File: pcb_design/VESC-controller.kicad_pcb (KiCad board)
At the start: 2 copper layers, 160 x 92.5 mm, 183 parts, among them J1 GATE_DRIVER_CONN_U, J2 GATE_DRIVER_CONN_V, J3 GATE_DRIVER_CONN_W, J4 micro USB, J5 ACCEL, J6 REGEN, J7 12V, P1 HALL/Encoder, P101 CANBUS, P3 PWR_COMM, Q1 BSC340N08, U1 STM32F40X_LQFP64, U10 LM2903-SO8, U11 LM3488, U12 OPA2376AID, U13 LM1117IMP-v.v, U16 OPA2376AID, U17 LM2903-SO8, U2 ISO1050, U3 OPA2376AID, U4 LM2903-SO8, U5 7400-TSSOP, U6 SN74ALVC08PWR, U7 SN74ALVC08PWR, U8 SN74AUP1G74, U9 LM22676QTJ-5.0, X2 ABM3B - 8MHz

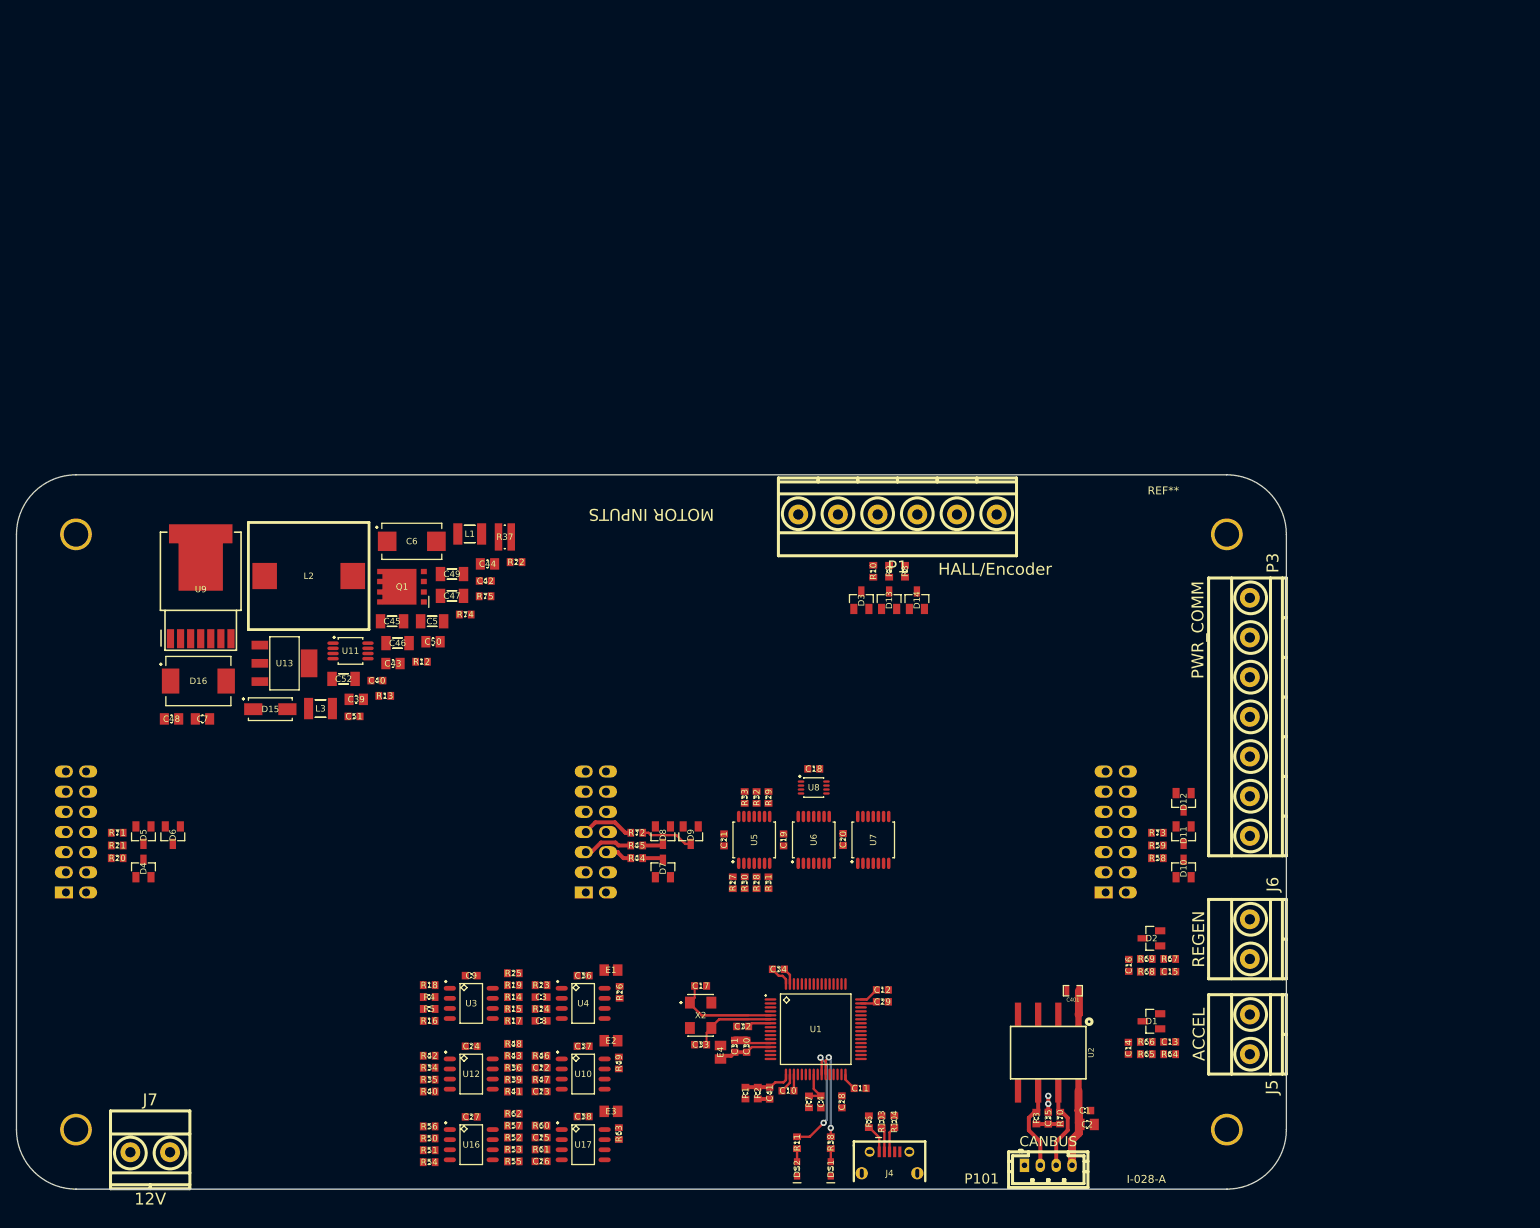
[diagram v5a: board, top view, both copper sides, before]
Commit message: Fixed issue with non-bidirectional phase current measurement. Started routing power supplies. Changed terminal blocks from 5.00mm to 3.81mm pitch
Signed-off-by: Marcos Chaparro <mchaparro@paltatech.com>
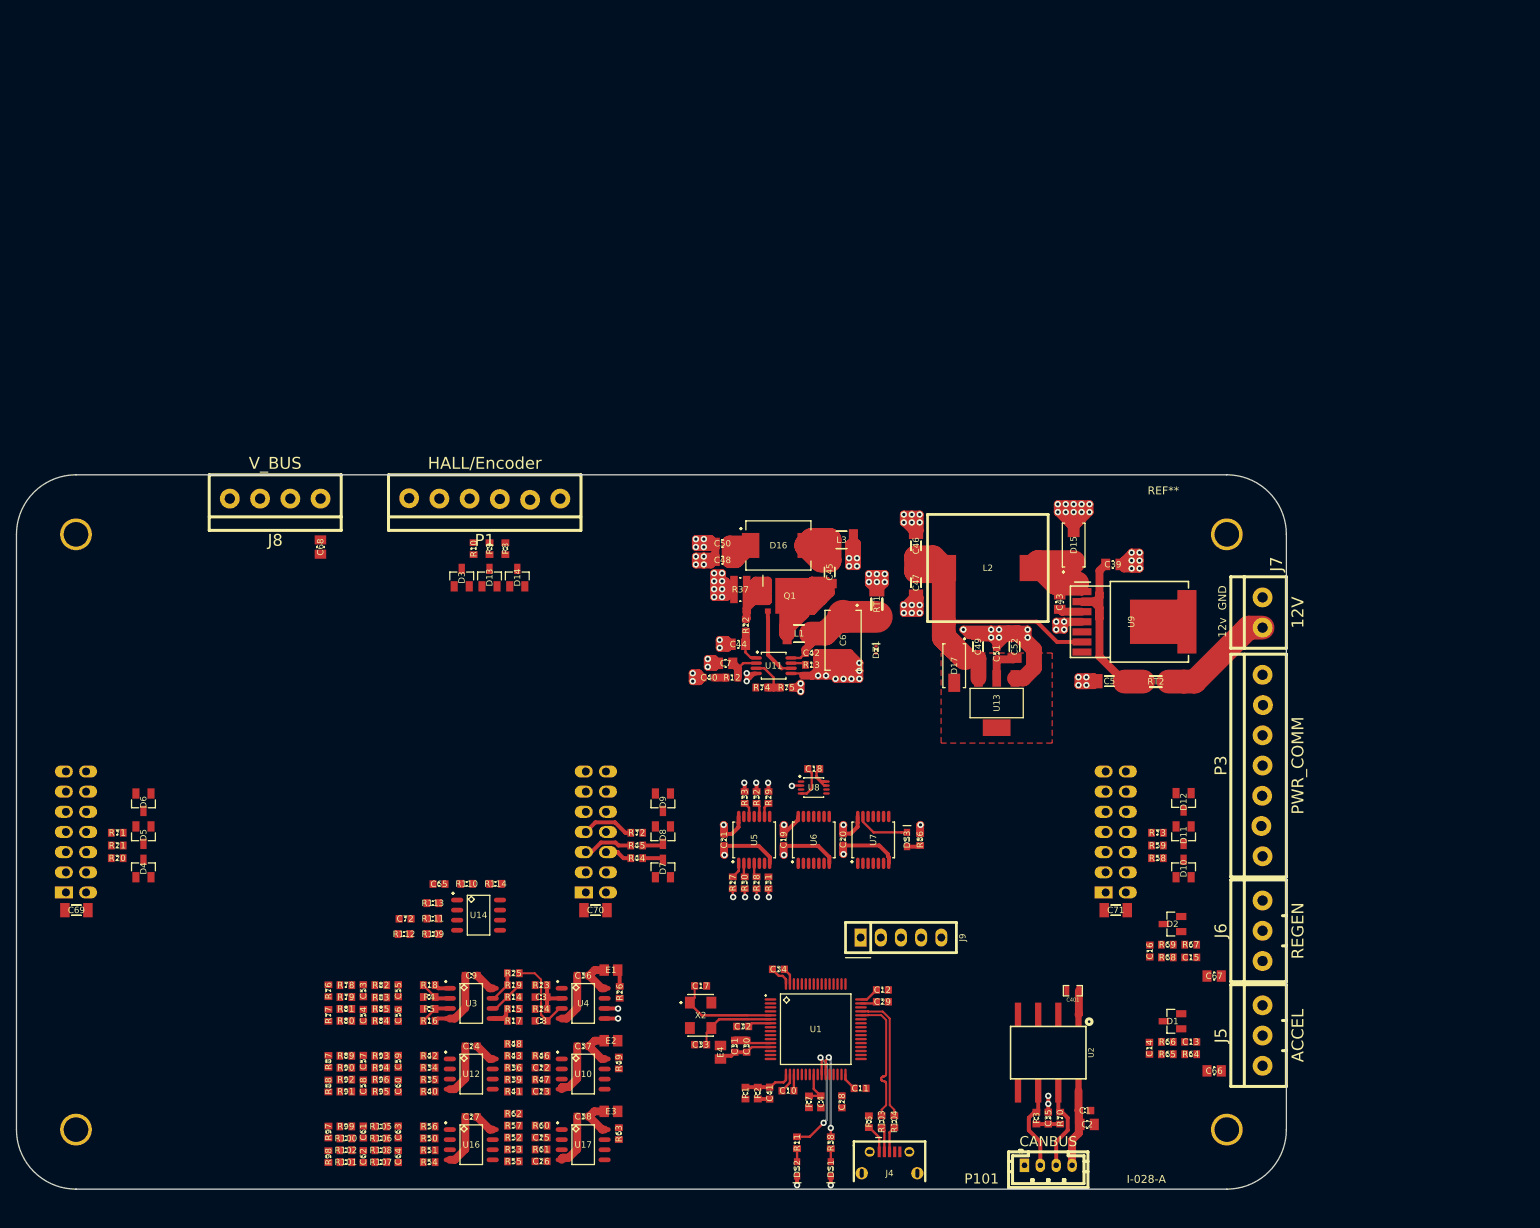
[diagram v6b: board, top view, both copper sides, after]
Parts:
- added C53: 100pF, IPC7351-Nominal:CAPC1608X55, F.Cu at (-36.3, 20.0)
- added C54: 100pF, IPC7351-Nominal:CAPC1608X55, F.Cu at (-36.3, 23.1)
- added C55: 100pF, IPC7351-Nominal:CAPC1608X55, F.Cu at (-31.9, 20.0)
- added C56: 100pF, IPC7351-Nominal:CAPC1608X55, F.Cu at (-31.9, 23.1)
- added C57: 100pF, IPC7351-Nominal:CAPC1608X55, F.Cu at (-36.3, 28.9)
- added C58: 100pF, IPC7351-Nominal:CAPC1608X55, F.Cu at (-36.3, 32.0)
- added C59: 100pF, IPC7351-Nominal:CAPC1608X55, F.Cu at (-31.9, 28.9)
- added C60: 100pF, IPC7351-Nominal:CAPC1608X55, F.Cu at (-31.9, 32.0)
- added C61: 100pF, IPC7351-Nominal:CAPC1608X55, F.Cu at (-36.3, 37.8)
- added C62: 100pF, IPC7351-Nominal:CAPC1608X55, F.Cu at (-36.3, 40.9)
- added C63: 100pF, IPC7351-Nominal:CAPC1608X55, F.Cu at (-31.9, 37.8)
- added C64: 100pF, IPC7351-Nominal:CAPC1608X55, F.Cu at (-31.9, 40.9)
- added C65: 100pF, IPC7351-Nominal:CAPC1608X55, F.Cu at (-26.8, 6.56)
- added C66: 4.7uF, IPC7351-Nominal:CAPC2012X70, F.Cu at (70.9, 30.1)
- added C67: 4.7uF, IPC7351-Nominal:CAPC2012X70, F.Cu at (70.9, 18.1)
- added C68: 4.7uF, IPC7351-Nominal:CAPC2012X70, F.Cu at (-41.7, -35.9)
- added C69: 4.7uF 50v, IPC7351-Nominal:CAPC3216X70, F.Cu at (-72.5, 9.85)
- added C70: 4.7uF 50v, IPC7351-Nominal:CAPC3216X70, F.Cu at (-7.05, 9.85)
- added C71: 4.7uF 50v, IPC7351-Nominal:CAPC3216X70, F.Cu at (58.5, 9.85)
- added C72: 100nF, IPC7351-Nominal:CAPC1608X55, F.Cu at (-31.0, 10.9)
- added D17: SS16, IPC7351-Nominal:DIOM5326X292, F.Cu at (38.1, -20.9)
- added DS3: OCP, smd-semi:LED-0603, F.Cu at (32.2, 0.95)
- added DZ1: ESD9L5.0ST5G, smd-semi:SOD-THAT, F.Cu at (28.3, -22.9)
- added J8: V_BUS, conn-phoenix:mcv_1,5-4-G-3,81, F.Cu at (-47.4, -42.0)
- added J9: SWD, conn-100mil:CONN-100MIL-M-1x5, F.Cu at (31.4, 13.3)
- added R100: 100R, IPC7351-Nominal:RESC1608X50, F.Cu at (-38.5, 38.6)
- added R101: 100R, IPC7351-Nominal:RESC1608X50, F.Cu at (-38.5, 41.6)
- added R102: 100R, IPC7351-Nominal:RESC1608X50, F.Cu at (-38.5, 40.1)
- added R105: 100R, IPC7351-Nominal:RESC1608X50, F.Cu at (-34.1, 37.1)
- added R106: 100R, IPC7351-Nominal:RESC1608X50, F.Cu at (-34.1, 38.6)
- added R107: 100R, IPC7351-Nominal:RESC1608X50, F.Cu at (-34.1, 41.6)
- added R108: 100R, IPC7351-Nominal:RESC1608X50, F.Cu at (-34.1, 40.1)
- added R109: 100R, IPC7351-Nominal:RESC1608X50, F.Cu at (-27.5, 12.9)
- added R110: 100R, IPC7351-Nominal:RESC1608X50, F.Cu at (-23.3, 6.54)
- added R111: 10k, IPC7351-Nominal:RESC1608X50, F.Cu at (-27.5, 10.9)
- added R112: 10k, IPC7351-Nominal:RESC1608X50, F.Cu at (-31.2, 12.9)
- added R113: 10k, IPC7351-Nominal:RESC1608X50, F.Cu at (-27.5, 8.97)
- added R114: 10k, IPC7351-Nominal:RESC1608X50, F.Cu at (-19.6, 6.54)
- added R76: 2k, IPC7351-Nominal:RESC1608X50, F.Cu at (-40.7, 20.0)
- added R77: 2k, IPC7351-Nominal:RESC1608X50, F.Cu at (-40.7, 23.1)
- added R78: 100R, IPC7351-Nominal:RESC1608X50, F.Cu at (-38.5, 19.3)
- added R79: 100R, IPC7351-Nominal:RESC1608X50, F.Cu at (-38.5, 20.8)
- added R80: 100R, IPC7351-Nominal:RESC1608X50, F.Cu at (-38.5, 23.8)
- added R81: 100R, IPC7351-Nominal:RESC1608X50, F.Cu at (-38.5, 22.3)
- added R82: 100R, IPC7351-Nominal:RESC1608X50, F.Cu at (-34.1, 19.3)
- added R83: 100R, IPC7351-Nominal:RESC1608X50, F.Cu at (-34.1, 20.8)
- added R84: 100R, IPC7351-Nominal:RESC1608X50, F.Cu at (-34.1, 23.8)
- added R85: 100R, IPC7351-Nominal:RESC1608X50, F.Cu at (-34.1, 22.3)
- added R86: 100R, IPC7351-Nominal:RESC1608X50, F.Cu at (33.9, 0.95)
- added R87: 2k, IPC7351-Nominal:RESC1608X50, F.Cu at (-40.7, 28.9)
- added R88: 2k, IPC7351-Nominal:RESC1608X50, F.Cu at (-40.7, 32.0)
- added R89: 100R, IPC7351-Nominal:RESC1608X50, F.Cu at (-38.5, 28.2)
- added R90: 100R, IPC7351-Nominal:RESC1608X50, F.Cu at (-38.5, 29.7)
- added R91: 100R, IPC7351-Nominal:RESC1608X50, F.Cu at (-38.5, 32.7)
- added R92: 100R, IPC7351-Nominal:RESC1608X50, F.Cu at (-38.5, 31.2)
- added R93: 100R, IPC7351-Nominal:RESC1608X50, F.Cu at (-34.1, 28.2)
- added R94: 100R, IPC7351-Nominal:RESC1608X50, F.Cu at (-34.1, 29.7)
- added R95: 100R, IPC7351-Nominal:RESC1608X50, F.Cu at (-34.1, 32.7)
- added R96: 100R, IPC7351-Nominal:RESC1608X50, F.Cu at (-34.1, 31.2)
- added R97: 2k, IPC7351-Nominal:RESC1608X50, F.Cu at (-40.7, 37.8)
- added R98: 2k, IPC7351-Nominal:RESC1608X50, F.Cu at (-40.7, 40.9)
- added R99: 100R, IPC7351-Nominal:RESC1608X50, F.Cu at (-38.5, 37.1)
- added RT1: POLYFUSE-30R500, IPC7351-Most:RESC3216X60, F.Cu at (28.4, -28.7)
- added RT2: POLYFUSE-30R500, IPC7351-Most:RESC3216X60, F.Cu at (63.5, -18.9)
- added U14: OPA2376AID, IPC7351-Nominal:SOIC127P600X175-8, F.Cu at (-21.8, 10.5)
- J5, J6: footprint w_conn_mkds:mkds_1,5-2 -> conn-phoenix:mcv_1,5-3-G-3,81
- J7: footprint w_conn_mkds:mkds_1,5-2 -> conn-phoenix:mcv_1,5-2-G-3,81
- P1: footprint w_conn_mkds:mkds_1,5-6 -> conn-phoenix:mcv_1,5-6-G-3,81
- P3: footprint w_conn_mkds:mkds_1,5-7 -> conn-phoenix:mcv_1,5-7-G-3,81
- REF**: footprint paltatech:VESC-controller-outline -> VESC-controller-outline
- moved J7 155.8 mm to (77.0, -27.6), turned to 90 degrees
- moved U9 117.3 mm to (60.5, -26.5), turned to 270 degrees
- moved D15 103.3 mm to (53.2, -36.1), turned to 90 degrees
- moved C39 96.8 mm to (58.1, -33.7)
- moved U13 89.9 mm to (43.5, -16.2), turned to 270 degrees
- moved C5 85.7 mm to (57.7, -19.0), turned to 180 degrees
- moved L2 85.6 mm to (42.4, -33.3)
- moved C52 84.6 mm to (45.8, -23.4), turned to 270 degrees
- moved C43 84.4 mm to (51.4, -29.0), turned to 270 degrees
- moved C51 81.4 mm to (43.5, -22.5), turned to 90 degrees
- moved D16 75.1 mm to (16.0, -36.1)
- moved C48 72.2 mm to (8.95, -34.2), turned to 180 degrees
- moved L3 69.0 mm to (23.9, -36.8), turned to 180 degrees
- moved C49 66.9 mm to (41.1, -23.4), turned to 90 degrees
- moved C46 66.5 mm to (33.3, -36.1), turned to 90 degrees
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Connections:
- net /STM32F4/SPI3_MISO renamed /STM32F4/PC11
- net /STM32F4/SPI3_SCK renamed /STM32F4/PC10
- net /STM32F4/USB_DM renamed /STM32F4/USB_D-
- net /STM32F4/USB_DP renamed /STM32F4/USB_D+
- net /Supervisor/DRIVER_RESET_OUT renamed /Supervisor/~DRIVER_RST_OUT
- net 24v renamed +24
- C10 pad 1: VCC -> +3.3
- C11 pad 1: VCC -> +3.3
- C12 pad 1: VCC -> +3.3
- C18 pad 2: VCC -> +3.3
- C19 pad 2: VCC -> +3.3
- C20 pad 2: VCC -> +3.3
- C21 pad 2: VCC -> +3.3
- C30 pad 1: Net-(C30-Pad1) -> +3.3A
- C31 pad 1: Net-(C30-Pad1) -> +3.3A
- C34 pad 1: VCC -> +3.3
- C39 pad 1: /Power/12v_in -> Net-(C39-Pad1)
- C401 pad 1: VCC -> +3.3
- C42 pad 1: /Power/12v_in -> Net-(C42-Pad1)
- C46 pad 1: 5.0v -> +5
- C47 pad 1: 5.0v -> +5
- C49 pad 1: 5.0v -> +5
- C5 pad 1: /Power/12v_in -> Net-(C39-Pad1)
- C51 pad 1: 3.3v -> +3.3
- C52 pad 2: 3.3v -> +3.3
- C6 pad 1: /Power/12v_in -> Net-(C42-Pad1)
- D10 pad 2: VCC -> +3.3
- D11 pad 2: VCC -> +3.3
- D12 pad 2: VCC -> +3.3
- D13 pad 2: VCC -> +3.3
- D14 pad 2: VCC -> +3.3
- D3 pad 2: VCC -> +3.3
- D4 pad 2: VCC -> +3.3
- D5 pad 2: VCC -> +3.3
- D6 pad 2: VCC -> +3.3
- D7 pad 2: VCC -> +3.3
- D8 pad 2: VCC -> +3.3
- D9 pad 2: VCC -> +3.3
- E1 pad 2: VCC -> +3.3
- E2 pad 2: VCC -> +3.3
- E3 pad 2: VCC -> +3.3
- E4 pad 1: Net-(C30-Pad1) -> +3.3A
- E4 pad 2: VCC -> +3.3
- J5 pad 1: /Accel input conditioning/IN -> +5
- J5 pad 2: GND -> /Accel input conditioning/IN
- J6 pad 1: /Regen input conditioning/IN -> +5
- J6 pad 2: GND -> /Regen input conditioning/IN
- L1 pad 2: /Power/12v_in -> Net-(C42-Pad1)
- L2 pad 1: 5.0v -> +5
- P1 pad 1: +5V -> +5
- P3 pad 1: +5V -> +5
- P3 pad 2: VCC -> +3.3
- R1 pad 1: VCC -> +3.3A
- R14 pad 2: /conditioning U/I_phase+ -> Net-(C56-Pad1)
- R15 pad 2: /conditioning U/I_phase- -> Net-(C56-Pad2)
- R26 pad 2: VCC -> +3.3
- R33 pad 1: VCC -> +3.3
- R34 pad 2: /conditioning V/V_phase+ -> Net-(C59-Pad1)
- R35 pad 2: /conditioning V/V_phase- -> Net-(C59-Pad2)
- R36 pad 2: /conditioning V/I_phase+ -> Net-(C60-Pad1)
- R39 pad 2: /conditioning V/I_phase- -> Net-(C60-Pad2)
- R4 pad 2: /conditioning U/V_phase+ -> Net-(C55-Pad1)
- R49 pad 2: VCC -> +3.3
- R5 pad 2: /conditioning U/V_phase- -> Net-(C55-Pad2)
- R50 pad 2: /conditioning W/V_phase+ -> Net-(C63-Pad1)
- R51 pad 2: /conditioning W/V_phase- -> Net-(C63-Pad2)
- R52 pad 2: /conditioning W/I_phase+ -> Net-(C64-Pad1)
- R53 pad 2: /conditioning W/I_phase- -> Net-(C64-Pad2)
- R6 pad 2: +5V -> +5
- R63 pad 2: VCC -> +3.3
- R7 pad 2: VCC -> +3.3
- U1 pad 1: VCC -> +3.3
- U1 pad 11: /STM32F4/AN_IN -> /Vbus_conditioning/OUT
- U1 pad 13: Net-(C30-Pad1) -> +3.3A
- U1 pad 19: VCC -> +3.3
- U1 pad 32: VCC -> +3.3
- U1 pad 33: /STM32F4/PB12 -> /STM32F4/~FAULT
- U1 pad 40: /STM32F4/SPI3_CS -> SUPPLY_SYNC
- U1 pad 48: VCC -> +3.3
- U1 pad 53: /STM32F4/SPI3_MOSI -> /Supervisor/CLR_OC_Fault
- U1 pad 56: /STM32F4/PB4 -> -VEE_ctrl
- U1 pad 58: -VEE_ctrl -> /STM32F4/PWM_AUX
- U1 pad 59: FAULT -> /Supervisor/OC_Fault
- U1 pad 64: VCC -> +3.3
- U10 pad 5: Net-(U10-Pad5) -> GND
- U10 pad 6: Net-(U10-Pad6) -> +3.3
- U11 pad 8: /Power/12v_in -> Net-(C42-Pad1)
- U13 pad 2: 3.3v -> +3.3
- U13 pad 3: 5.0v -> +5
- U13 pad 4: 3.3v -> +3.3
- U17 pad 5: Net-(U17-Pad5) -> GND
- U17 pad 6: Net-(U17-Pad6) -> +3.3
- U2 pad 1: VCC -> +3.3
- U4 pad 5: Net-(U4-Pad5) -> GND
- U4 pad 6: Net-(U4-Pad6) -> +3.3
- U5 pad 14: VCC -> +3.3
- U6 pad 14: VCC -> +3.3
- U7 pad 10: FAULT -> /STM32F4/~FAULT
- U7 pad 14: VCC -> +3.3
- U7 pad 9: /Supervisor/DRIVER_RESET_IN -> /STM32F4/~DRIVER_RESET
- U8 pad 2: VCC -> +3.3
- U8 pad 6: /Supervisor/CLEAR_OC_Fault -> /Supervisor/CLR_OC_Fault
- U8 pad 7: VCC -> +3.3
- U8 pad 8: VCC -> +3.3
- U9 pad 2: /Power/12v_in -> Net-(C39-Pad1)
- U9 pad 6: 5.0v -> +5
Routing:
- net GND: track 10.7 -> 315.7 mm, vias 0 -> 93
- net /Power/12v_in: track 0.00 -> 92.0 mm, vias 0 -> 6
- net +5: track 0.00 -> 46.5 mm
- net +3.3: track 0.00 -> 43.1 mm, vias 0 -> 7
- net Net-(C45-Pad2): track 0.00 -> 40.0 mm
- net Net-(C39-Pad1): track 0.00 -> 25.6 mm
- net Net-(Q1-Pad1): track 0.00 -> 25.0 mm
- net /STM32F4/USB_D-: track 0.00 -> 16.5 mm
- net /STM32F4/USB_D+: track 0.00 -> 16.5 mm
- net Net-(C43-Pad1): track 0.00 -> 16.4 mm
- net Net-(C42-Pad1): track 0.00 -> 14.1 mm
- net Net-(C8-Pad1): track 0.00 -> 12.6 mm
- net VCC: track 12.6 -> 0.00 mm
- net Net-(C45-Pad1): track 0.00 -> 9.58 mm
- net Net-(Q1-Pad4): track 0.00 -> 9.16 mm
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- added copper zone on F.Cu, net +3.3
- added copper zone on PWR.Cu, net +3.3
- added copper zone on GND.Cu, net GND
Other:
- board size 160 x 92.5 mm -> 160 x 90 mm
- copper layers 2 -> 4
- rule pad_to_mask_clearance: 0.2 -> 0.15
- board text added: "12v"
- board text added: "GND"
- board text removed: "MOTOR INPUTS"

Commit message: More layout
Signed-off-by: Marcos Chaparro <mchaparro@paltatech.com>
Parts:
- added P2: Resolver, conn-phoenix:mcv_1,5-6-G-3,81, F.Cu at (-5.00, -42.0)
- added R115: 1k, IPC7351-Nominal:RESC1608X50, F.Cu at (-16.2, 34.4)
- added R116: 1k, IPC7351-Nominal:RESC1608X50, F.Cu at (-16.2, 37.2)
- added R117: 1k, IPC7351-Nominal:RESC1608X50, F.Cu at (-16.2, 25.6)
- added R118: 1k, IPC7351-Nominal:RESC1608X50, F.Cu at (-16.2, 28.7)
- added R119: 1k, IPC7351-Nominal:RESC1608X50, F.Cu at (-16.9, 17.2)
- added R120: 1k, IPC7351-Nominal:RESC1608X50, F.Cu at (-16.9, 20.1)
- added R121: 2k, IPC7351-Nominal:RESC1608X50, F.Cu at (-36.1, 7.95)
- added R122: 1k, IPC7351-Nominal:RESC1608X50, F.Cu at (23.4, 13.2)
- J1, J2, J3: footprint conn-100mil:CONN-100MIL-M-2x7 -> conn-100mil:CONN-100MIL-M-2x8
- R17, R41, R55: value R-0603 -> 9.5k
- moved R50 20.8 mm to (-29.8, 17.9)
- moved R51 20.8 mm to (-29.8, 19.4)
- moved R54 20.8 mm to (-29.8, 20.9)
- moved R56 20.8 mm to (-29.8, 16.4)
- moved C27 20.8 mm to (-24.4, 15.2)
- moved R52 20.8 mm to (-19.1, 17.8)
- moved R53 20.8 mm to (-19.1, 19.3)
- moved R55 20.8 mm to (-19.1, 20.8)
- moved R57 20.8 mm to (-19.1, 16.3)
- moved R62 20.8 mm to (-19.1, 14.8)
- moved U16 20.8 mm to (-24.4, 18.7)
- moved R100 20.7 mm to (-39.5, 17.9)
- moved R101 20.7 mm to (-39.5, 20.9)
- moved R102 20.7 mm to (-39.5, 19.4)
- moved R105 20.7 mm to (-35.1, 16.4)
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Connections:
- net Net-(C55-Pad1) renamed /conditioning U/V_diff_+
- net Net-(C55-Pad2) renamed /conditioning U/V_diff_-
- net Net-(C56-Pad1) renamed /conditioning U/I_diff_+
- net Net-(C56-Pad2) renamed /conditioning U/I_diff_-
- net Net-(C59-Pad1) renamed /conditioning V/V_diff_+
- net Net-(C59-Pad2) renamed /conditioning V/V_diff_-
- net Net-(C60-Pad1) renamed /conditioning V/I_diff_+
- net Net-(C60-Pad2) renamed /conditioning V/I_diff_-
- net Net-(C63-Pad1) renamed /conditioning W/V_diff_+
- net Net-(C63-Pad2) renamed /conditioning W/V_diff_-
- net Net-(C64-Pad1) renamed /conditioning W/I_diff_+
- net Net-(C64-Pad2) renamed /conditioning W/I_diff_-
- R17 pad 1: GND -> Net-(R115-Pad2)
- R41 pad 1: GND -> Net-(R117-Pad2)
- R55 pad 1: GND -> Net-(R119-Pad2)
- U1 pad 33: /STM32F4/~FAULT -> ~FAULT
- U1 pad 60: GND -> Net-(R122-Pad1)
- U7 pad 10: /STM32F4/~FAULT -> ~FAULT
- U7 pad 11: /Supervisor/~DRIVER_RST_OUT -> ~DRIVER_RESET
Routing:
- net GND: track 315.7 -> 528.3 mm, vias 93 -> 183
- net ~DRIVER_RESET: track 0.00 -> 153.0 mm, vias 0 -> 1
- net ~FAULT: track 0.00 -> 151.7 mm, vias 0 -> 1
- net SUPPLY_SYNC: track 0.00 -> 146.5 mm
- net /conditioning W/I_phase+: track 0.00 -> 141.0 mm
- net -VEE_ctrl: track 0.00 -> 140.0 mm
- net /conditioning W/I_phase-: track 0.00 -> 138.4 mm
- net /conditioning W/V_phase-: track 0.00 -> 125.1 mm
- net /conditioning W/V_phase+: track 0.00 -> 123.6 mm
- net +3.3: track 43.1 -> 147.8 mm, vias 7 -> 60
- net /conditioning V/I_phase+: track 0.00 -> 91.4 mm
- net /conditioning V/I_phase-: track 0.00 -> 89.2 mm
- net /conditioning U/V_phase+: track 0.00 -> 86.8 mm
- net /conditioning U/V_phase-: track 0.00 -> 86.3 mm
- net /conditioning U/OC_Fault: track 0.00 -> 85.7 mm, vias 0 -> 7
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- added copper zone on GND.Cu, net /Isolated CAN/GND_CAN
- added copper zone on F.Cu, net GND
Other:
- board text added: "github.com/paltatech/VESC-controller"
